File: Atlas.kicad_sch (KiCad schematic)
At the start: 45 parts, among them J101 Conn_01x08_MountingPin, J102 BATT, J103 GND, U101 LMR51420YDDCR, U102 TLV76733DRVR, U103 INA186A2

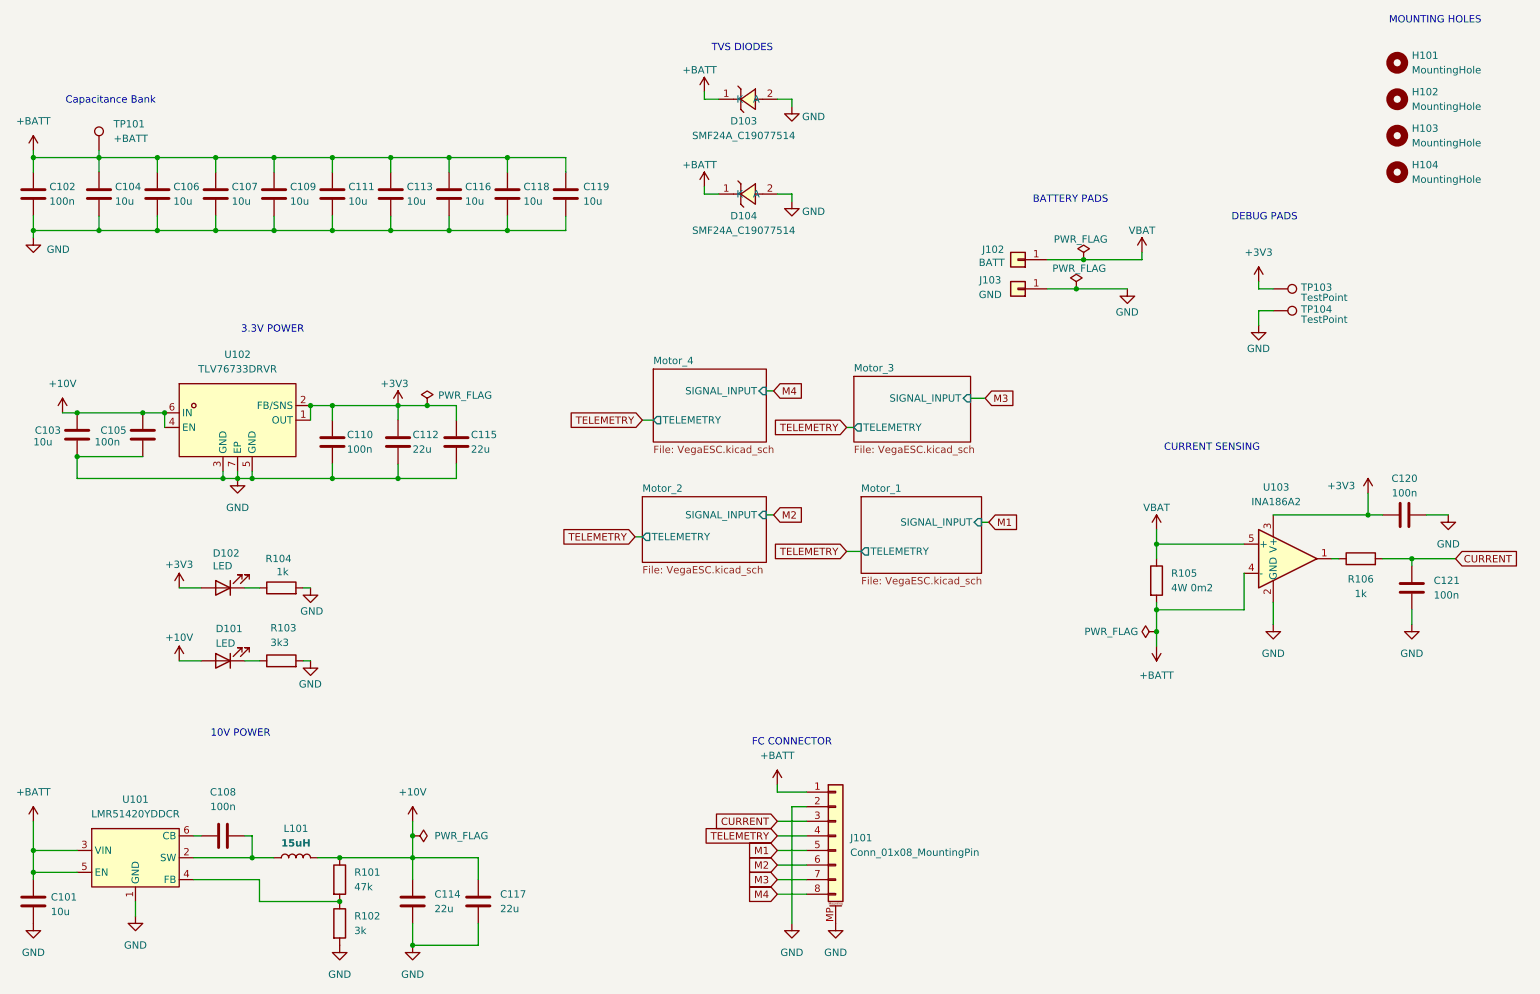
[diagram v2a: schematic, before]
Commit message: Refactor schematic: update MCU to AT32F421G8U7 (QFN-28), update footprints, and re-annotate designators
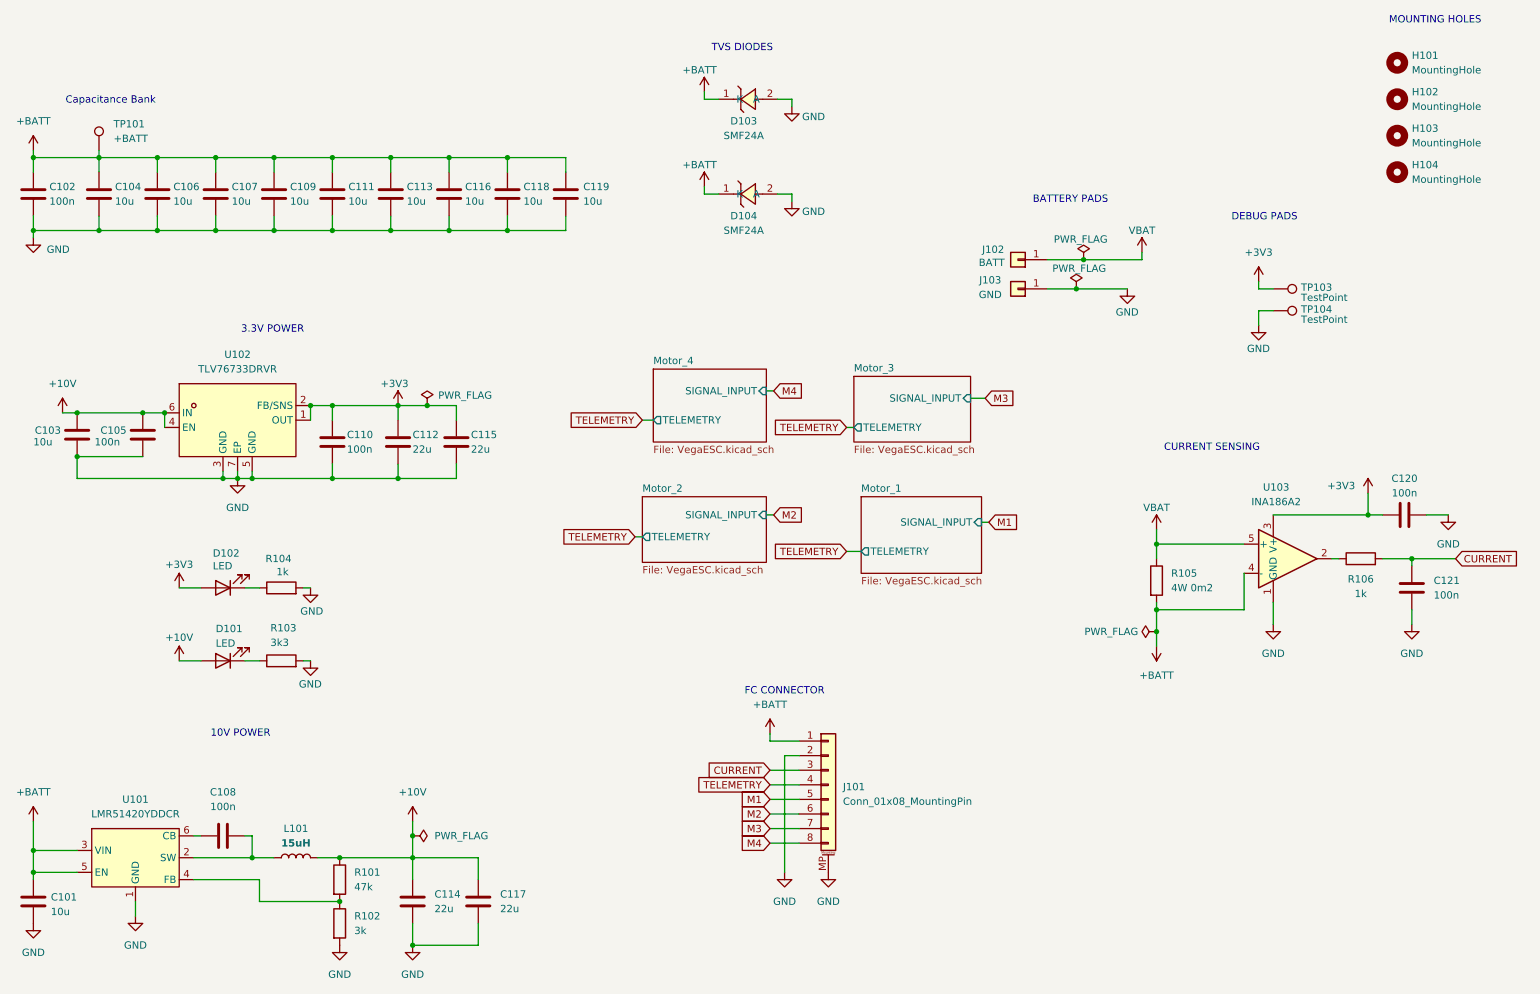
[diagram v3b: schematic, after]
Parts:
- D103: value SMF24A_C19077514 -> SMF24A; footprint easyeda2kicad:SOD-123FL_L2.7-W1.8-LS3.8-RD -> Diode_SMD:D_SOD-123F; lcsc C19077514 -> (none)
- D104: value SMF24A_C19077514 -> SMF24A; lcsc C19077514 -> (none)
- J101: MPN SM08B-SRSS-TB(LF)(SN) -> (none); Manufacturer JST -> (none); lcsc C160401 -> (none)
- L101: footprint easyeda2kicad:IND-SMD_L7.1-W6.6 -> Inductor_SMD:L_KOHERelec_MDA7030
- R105: MPN HOLR2725D-4W-0.2MR-1% -> (none)
- U103: footprint 4in1ESC:SOT-23-5_L2.9-W1.6-P0.95-LS2.8-BR -> easyeda2kicad:SOT-23-5_L2.9-W1.6-P0.94-LS2.8-BL
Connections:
- net GND: now also U103.1 (GND); no longer U103.2 (GND)
- net at R106.1: now also U103.2; no longer U103.1
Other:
- moved on the sheet: J101
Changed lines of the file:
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@@
 	(text "FC CONNECTOR"
 		(exclude_from_sim no)
-		(at 153.67 151.384 0)
+		(at 152.4 142.494 0)
 		(effects
 			(font
@@
 	(wire
 		(pts
-			(xy 151.13 175.26) (xy 156.21 175.26)
+			(xy 149.86 166.37) (xy 154.94 166.37)
 		)
 		(stroke
@@
 	(wire
 		(pts
-			(xy 151.13 158.75) (xy 151.13 160.02)
+			(xy 149.86 149.86) (xy 149.86 151.13)
 		)
 		(stroke
@@
 	(wire
 		(pts
-			(xy 151.13 165.1) (xy 156.21 165.1)
+			(xy 149.86 156.21) (xy 154.94 156.21)
 		)
 		(stroke
@@
 	(wire
 		(pts
-			(xy 151.13 172.72) (xy 156.21 172.72)
+			(xy 149.86 163.83) (xy 154.94 163.83)
 		)
 		(stroke
@@
 	(wire
 		(pts
-			(xy 151.13 170.18) (xy 156.21 170.18)
+			(xy 149.86 161.29) (xy 154.94 161.29)
 		)
 		(stroke
@@
 	(wire
 		(pts
-			(xy 153.67 162.56) (xy 153.67 182.88)
+			(xy 152.4 153.67) (xy 152.4 173.99)
 		)
 		(stroke
@@
 	(wire
 		(pts
-			(xy 151.13 177.8) (xy 156.21 177.8)
+			(xy 149.86 168.91) (xy 154.94 168.91)
 		)
 		(stroke
@@
 	(wire
 		(pts
-			(xy 151.13 160.02) (xy 156.21 160.02)
+			(xy 149.86 151.13) (xy 154.94 151.13)
 		)
 		(stroke
@@
 	(wire
 		(pts
-			(xy 151.13 167.64) (xy 156.21 167.64)
+			(xy 149.86 158.75) (xy 154.94 158.75)
 		)
 		(stroke
@@
 	(wire
 		(pts
-			(xy 156.21 162.56) (xy 153.67 162.56)
+			(xy 154.94 153.67) (xy 152.4 153.67)
 		)
 		(stroke
@@
 	(global_label "M1"
 		(shape input)
-		(at 151.13 170.18 180)
+		(at 149.86 161.29 180)
 		(fields_autoplaced yes)
 		(effects
@@
 		)
 		(property "Intersheetrefs" "${INTERSHEET_REFS}"
-			(at 145.4839 170.18 0)
+			(at 144.2139 161.29 0)
 			(hide yes)
 			(show_name no)
@@
 	(global_label "M3"
 		(shape input)
-		(at 151.13 175.26 180)
+		(at 149.86 166.37 180)
 		(fields_autoplaced yes)
 		(effects
@@
 		)
 		(property "Intersheetrefs" "${INTERSHEET_REFS}"
-			(at 145.4839 175.26 0)
+			(at 144.2139 166.37 0)
 			(hide yes)
 			(show_name no)
@@
 	(global_label "CURRENT"
 		(shape input)
-		(at 151.13 165.1 180)
+		(at 149.86 156.21 180)
 		(fields_autoplaced yes)
 		(effects
@@
 		)
 		(property "Intersheetrefs" "${INTERSHEET_REFS}"
-			(at 139.5572 165.1 0)
+			(at 138.2872 156.21 0)
 			(hide yes)
 			(show_name no)
@@
 	(global_label "M4"
 		(shape input)
-		(at 151.13 177.8 180)
+		(at 149.86 168.91 180)
 		(fields_autoplaced yes)
 		(effects
@@
 		)
 		(property "Intersheetrefs" "${INTERSHEET_REFS}"
-			(at 145.4839 177.8 0)
+			(at 144.2139 168.91 0)
 			(hide yes)
 			(show_name no)
@@
 	(global_label "TELEMETRY"
 		(shape input)
-		(at 151.13 167.64 180)
+		(at 149.86 158.75 180)
 		(fields_autoplaced yes)
 		(effects
@@
 		)
 		(property "Intersheetrefs" "${INTERSHEET_REFS}"
-			(at 137.9245 167.64 0)
+			(at 136.6545 158.75 0)
 			(hide yes)
 			(show_name no)
@@
 	(global_label "M2"
 		(shape input)
-		(at 151.13 172.72 180)
+		(at 149.86 163.83 180)
 		(fields_autoplaced yes)
 		(effects
@@
 		)
 		(property "Intersheetrefs" "${INTERSHEET_REFS}"
-			(at 145.4839 172.72 0)
+			(at 144.2139 163.83 0)
 			(hide yes)
 			(show_name no)
@@
 	(symbol
 		(lib_id "power:GND")
-		(at 161.29 182.88 0)
+		(at 160.02 173.99 0)
 		(unit 1)
 		(body_style 1)
@@
 		(fields_autoplaced yes)
 		(property "Reference" "#PWR0121"
-			(at 161.29 189.23 0)
+			(at 160.02 180.34 0)
 			(hide yes)
 			(show_name no)
@@
 		)
 		(property "Value" "GND"
-			(at 161.29 187.96 0)
+			(at 160.02 179.07 0)
 			(show_name no)
 			(do_not_autoplace no)
@@
 		)
 		(property "Footprint" ""
-			(at 161.29 182.88 0)
+			(at 160.02 173.99 0)
 			(hide yes)
 			(show_name no)
@@
 		)
 		(property "Datasheet" ""
-			(at 161.29 182.88 0)
+			(at 160.02 173.99 0)
 			(hide yes)
 			(show_name no)
@@
 		)
 		(property "Description" "Power symbol creates a global label with name \"GND\" , ground"
-			(at 161.29 182.88 0)
+			(at 160.02 173.99 0)
 			(hide yes)
 			(show_name no)
@@
 			)
 		)
-		(property "MPN" "HOLR2725D-4W-0.2MR-1%"
+		(property "MPN" ""
 			(at 167.64 -60.96 0)
 			(hide yes)
@@
 	(symbol
 		(lib_id "power:GND")
-		(at 153.67 182.88 0)
+		(at 152.4 173.99 0)
 		(unit 1)
 		(body_style 1)
@@
 		(fields_autoplaced yes)
 		(property "Reference" "#PWR0120"
-			(at 153.67 189.23 0)
+			(at 152.4 180.34 0)
 			(hide yes)
 			(show_name no)
@@
 		)
 		(property "Value" "GND"
-			(at 153.67 187.96 0)
+			(at 152.4 179.07 0)
 			(show_name no)
 			(do_not_autoplace no)
@@
 		)
 		(property "Footprint" ""
-			(at 153.67 182.88 0)
+			(at 152.4 173.99 0)
 			(hide yes)
 			(show_name no)
@@
 		)
 		(property "Datasheet" ""
-			(at 153.67 182.88 0)
+			(at 152.4 173.99 0)
 			(hide yes)
 			(show_name no)
@@
 		)
 		(property "Description" "Power symbol creates a global label with name \"GND\" , ground"
-			(at 153.67 182.88 0)
+			(at 152.4 173.99 0)
 			(hide yes)
 			(show_name no)
@@
 			)
 		)
-		(property "Value" "SMF24A_C19077514"
+		(property "Value" "SMF24A"
 			(at 145.288 62.23 0)
 			(show_name no)
@@
 			)
 		)
-		(property "lcsc" "C19077514" (at 0 0 0)
-			(effects
-				(font
-					(size 1.27 1.27)
-				)
-				(hide yes)
-			)
-		)
 		(pin "2"
 		)
@@
 	(symbol
 		(lib_id "power:+BATT")
-		(at 151.13 158.75 0)
+		(at 149.86 149.86 0)
 		(unit 1)
 		(body_style 1)
@@
 		(fields_autoplaced yes)
 		(property "Reference" "#PWR0119"
-			(at 151.13 162.56 0)
+			(at 149.86 153.67 0)
 			(hide yes)
 			(show_name no)
@@
 		)
 		(property "Value" "+BATT"
-			(at 151.13 153.67 0)
+			(at 149.86 144.78 0)
 			(show_name no)
 			(do_not_autoplace no)
@@
 		)
 		(property "Footprint" ""
-			(at 151.13 158.75 0)
+			(at 149.86 149.86 0)
 			(hide yes)
 			(show_name no)
@@
 		)
 		(property "Datasheet" ""
-			(at 151.13 158.75 0)
+			(at 149.86 149.86 0)
 			(hide yes)
 			(show_name no)
@@
 		)
 		(property "Description" "Power symbol creates a global label with name \"+BATT\""
-			(at 151.13 158.75 0)
+			(at 149.86 149.86 0)
 			(hide yes)
 			(show_name no)
@@
 			)
 		)
-		(property "Footprint" "4in1ESC:SOT-23-5_L2.9-W1.6-P0.95-LS2.8-BR"
+		(property "Footprint" "easyeda2kicad:SOT-23-5_L2.9-W1.6-P0.94-LS2.8-BL"
 			(at 241.3 118.11 0)
 			(hide yes)
@@
 			)
 		)
-		(property "Footprint" "easyeda2kicad:IND-SMD_L7.1-W6.6"
+		(property "Footprint" "Inductor_SMD:L_KOHERelec_MDA7030"
 			(at 67.31 171.45 0)
 			(hide yes)
@@
 			)
 		)
-		(property "Value" "SMF24A_C19077514"
+		(property "Value" "SMF24A"
 			(at 145.288 45.72 0)
 			(show_name no)
@@
 			)
 		)
-		(property "Footprint" "easyeda2kicad:SOD-123FL_L2.7-W1.8-LS3.8-RD"
+		(property "Footprint" "Diode_SMD:D_SOD-123F"
 			(at 146.05 46.99 0)
 			(hide yes)
@@
 			)
 		)
-		(property "lcsc" "C19077514" (at 0 0 0)
-			(effects
-				(font
-					(size 1.27 1.27)
-				)
-				(hide yes)
-			)
-		)
 		(pin "2"
 		)
@@
 	(symbol
 		(lib_id "Connector_Generic_MountingPin:Conn_01x08_MountingPin")
-		(at 161.29 167.64 0)
+		(at 160.02 158.75 0)
 		(unit 1)
 		(body_style 1)
@@
 		(fields_autoplaced yes)
 		(property "Reference" "J101"
-			(at 163.83 167.9955 0)
+			(at 162.56 159.1055 0)
 			(show_name no)
 			(do_not_autoplace no)
@@
 		)
 		(property "Value" "Conn_01x08_MountingPin"
-			(at 163.83 170.5355 0)
+			(at 162.56 161.6455 0)
 			(show_name no)
 			(do_not_autoplace no)
@@
 		)
 		(property "Footprint" "Connector_JST:JST_SH_SM08B-SRSS-TB_1x08-1MP_P1.00mm_Horizontal"
-			(at 161.29 167.64 0)
+			(at 160.02 158.75 0)
 			(hide yes)
 			(show_name no)
@@
 			)
 		)
-		(property "Datasheet" "https://datasheet.lcsc.com/datasheet/pdf/2304141430_JST-SM08B-SRSS-TB-LF-SN_C160401.pdf"
-			(at 161.29 167.64 0)
+		(property "Datasheet" ""
+			(at 160.02 158.75 0)
 			(hide yes)
 			(show_name no)
@@
 		)
 		(property "Description" "Generic connectable mounting pin connector, single row, 01x08, script generated (kicad-library-utils/schlib/autogen/connector/)"
-			(at 161.29 167.64 0)
+			(at 160.02 158.75 0)
 			(hide yes)
 			(show_name no)
@@
 			)
 		)
-		(property "lcsc" "C160401" (at 0 0 0)
-			(effects
-				(font
-					(size 1.27 1.27)
-				)
-				(hide yes)
-			)
-		)
-		(property "Manufacturer" "JST" (at 0 0 0)
-			(effects
-				(font
-					(size 1.27 1.27)
-				)
-				(hide yes)
-			)
-		)
-		(property "MPN" "SM08B-SRSS-TB(LF)(SN)" (at 0 0 0)
-			(effects
-				(font
-					(size 1.27 1.27)
-				)
-				(hide yes)
-			)
-		)

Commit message: Stage user updates for MOSFET pinouts and MCU footprints, and update design review
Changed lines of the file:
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@@
 	(text "10V POWER"
 		(exclude_from_sim no)
-		(at 57.658 149.86 0)
+		(at 58.42 153.162 0)
 		(effects
 			(font
@@
 				(font
 					(size 1.27 1.27)
-					(thickness 0.254)
-					(bold yes)
+					(thickness 0.1588)
 				)
 			)
